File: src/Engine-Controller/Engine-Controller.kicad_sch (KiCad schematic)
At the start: 19 parts, among them J2 Jumper_NO, P3 3220-20-0200-00, U1 STM32H750VBTx, Y1 ECS-240-18-33-JGN-TR

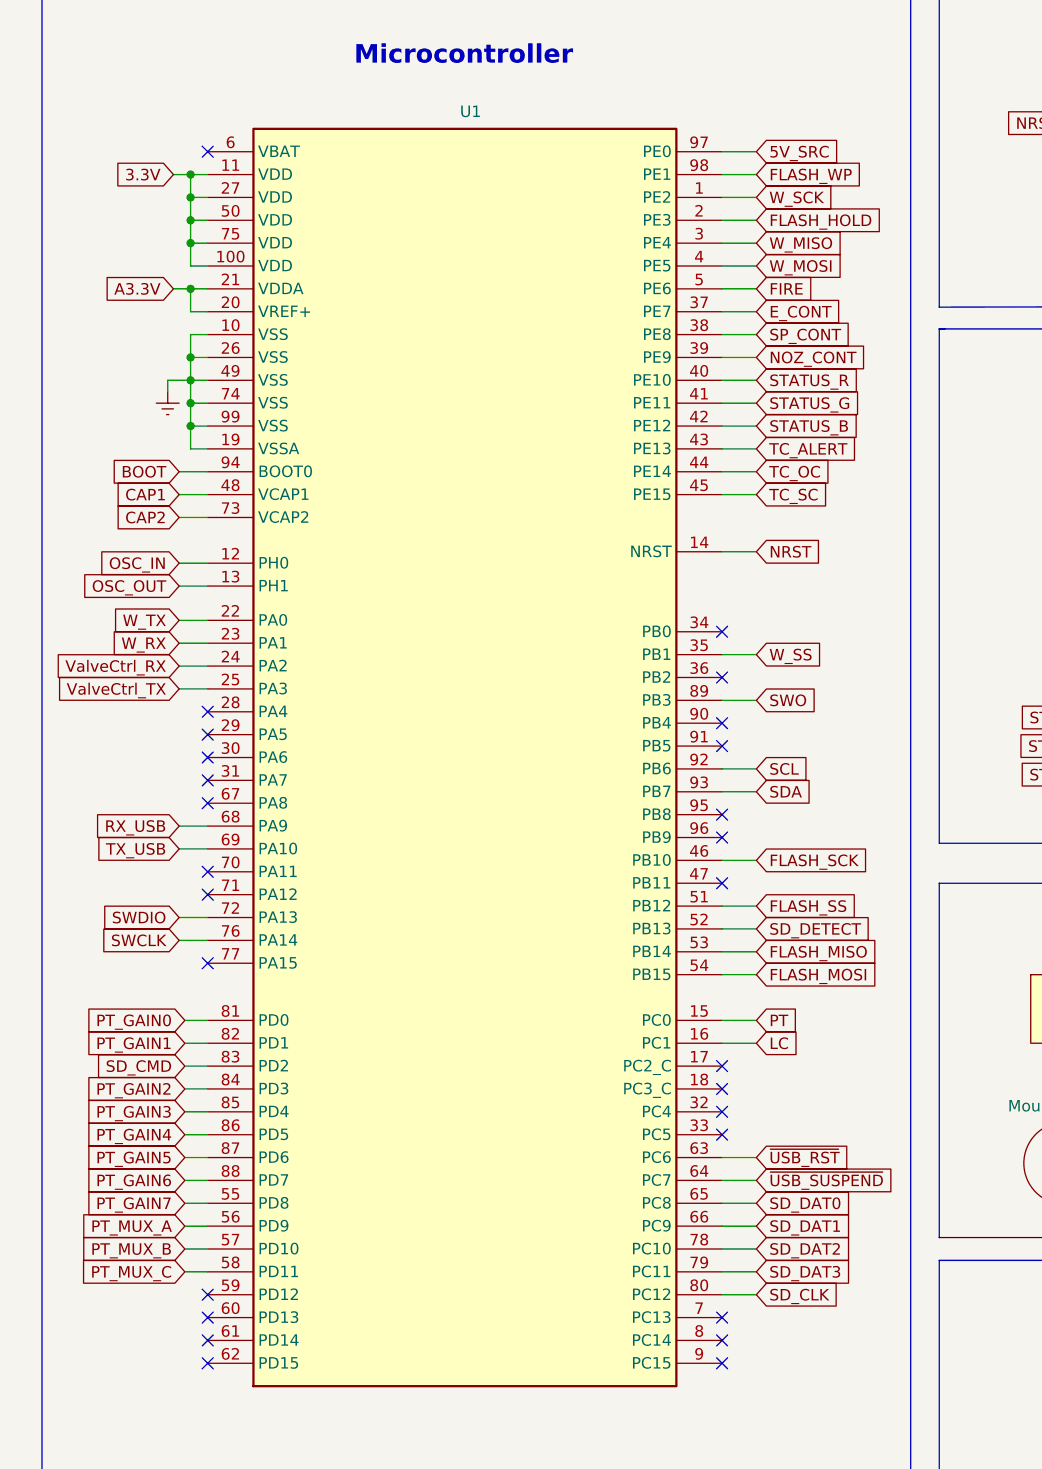
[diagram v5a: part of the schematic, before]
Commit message: removed uncessary caps from MCU LDO pins
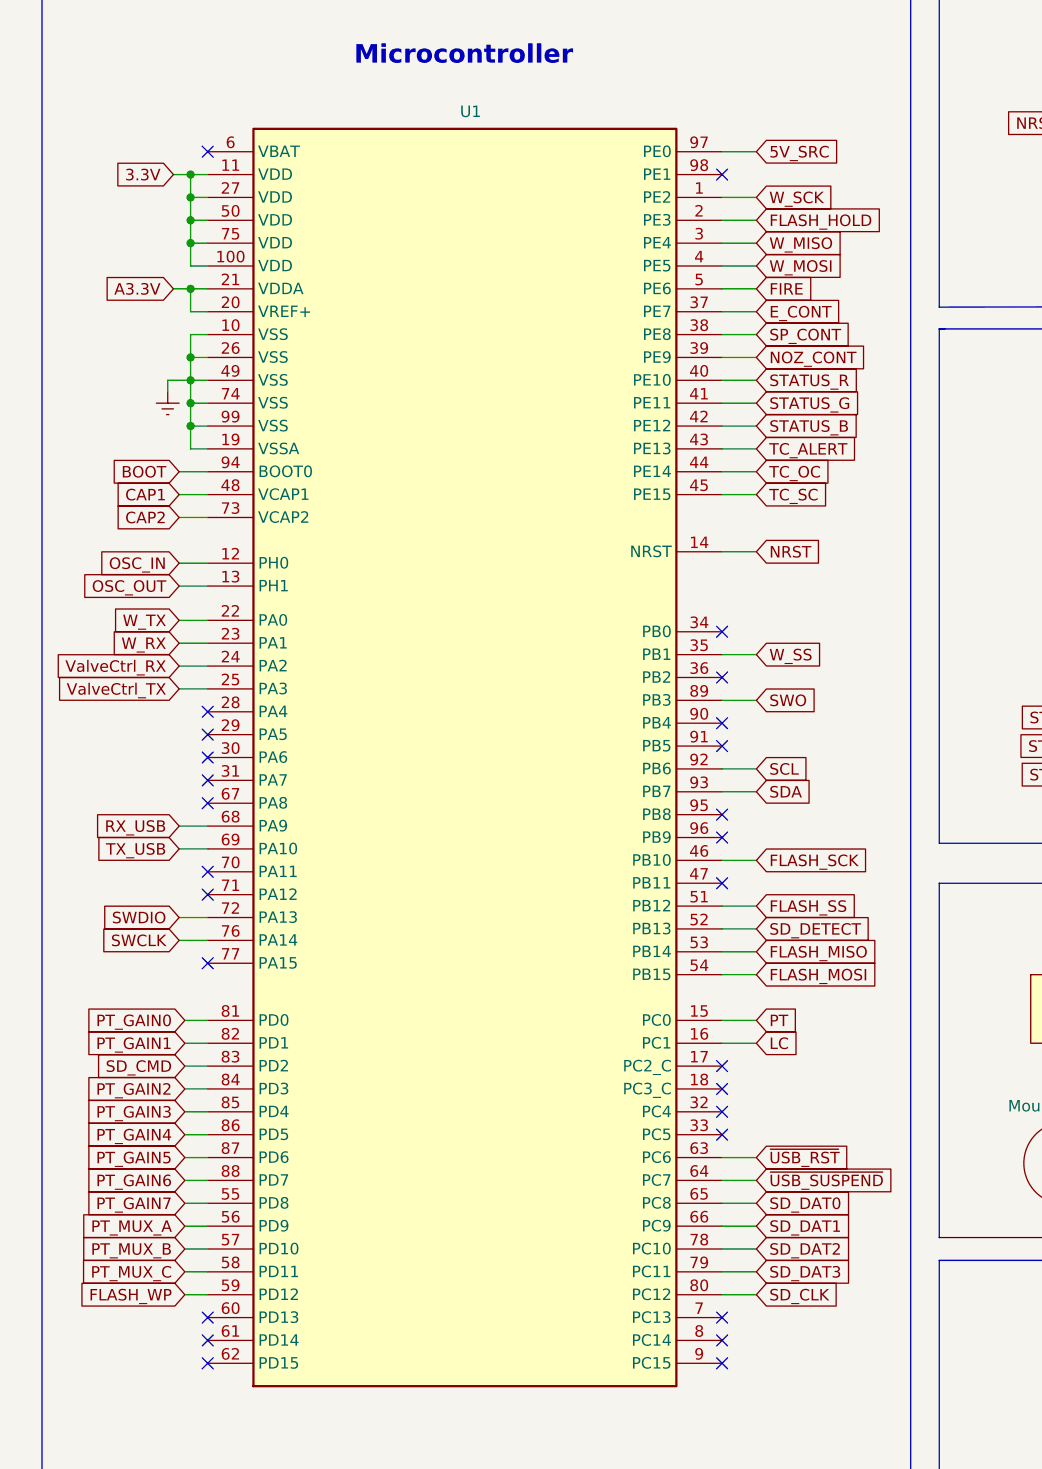
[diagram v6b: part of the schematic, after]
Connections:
- net FLASH_WP: now also U1.59 (PD12); no longer U1.98 (PE1)
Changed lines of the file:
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@@
   (no_connect (at 34.29 106.68))
   (no_connect (at 34.29 111.76))
+  (no_connect (at 91.44 41.91))
   (no_connect (at 91.44 113.03))
-  (no_connect (at 34.29 166.37))
   (no_connect (at 160.655 43.815))
   (no_connect (at 160.655 36.195))
@@
     (stroke (width 0) (type default) (color 0 0 0 0))
   )
-  (wire (pts (xy 91.44 41.91) (xy 95.25 41.91))
-    (stroke (width 0) (type default) (color 0 0 0 0))
-  )
   (wire (pts (xy 201.295 97.155) (xy 204.47 97.155))
     (stroke (width 0) (type default) (color 0 0 0 0))
@@
   )
   (wire (pts (xy 91.44 67.31) (xy 95.25 67.31))
+    (stroke (width 0) (type default) (color 0 0 0 0))
+  )
+  (wire (pts (xy 31.75 166.37) (xy 34.29 166.37))
     (stroke (width 0) (type default) (color 0 0 0 0))
   )
@@
     )
   )
-  (global_label "FLASH_WP" (shape input) (at 95.25 41.91 0) (fields_autoplaced)
-    (effects (font (size 1.27 1.27)) (justify left))
-    (property "Intersheet References" "${INTERSHEET_REFS}" (id 0) (at -43.18 5.08 0)
+  (global_label "FLASH_WP" (shape input) (at 31.75 166.37 180) (fields_autoplaced)
+    (effects (font (size 1.27 1.27)) (justify right))
+    (property "Intersheet References" "${INTERSHEET_REFS}" (id 0) (at 170.18 203.2 0)
       (effects (font (size 1.27 1.27)) hide)
     )
@@
       (reference "#PWR0109") (unit 1) (value "Earth") (footprint "")
     )
+    (path "/00000000-0000-0000-0000-000060d7f309/59b043bf-a20d-42bd-97fc-7a18b415d9ac"
+      (reference "#PWR?") (unit 1) (value "Earth") (footprint "")
+    )
+    (path "/00000000-0000-0000-0000-000060d7f309/64a6fbd3-18d0-41d3-87fa-96e96c558542"
+      (reference "#PWR?") (unit 1) (value "Earth") (footprint "")
+    )
     (path "/00000000-0000-0000-0000-0000610156a4"
       (reference "B1") (unit 1) (value "PTS647SM38SMTR2LFS") (footprint "Engine-Controller:PTS647SM38SMTR2LFS")
@@
       (reference "C23") (unit 1) (value "2.2uF") (footprint "Engine-Controller:CAP_0603")
     )
-    (path "/00000000-0000-0000-0000-000060d7f309/b8efbc02-3ff5-4b40-a4ff-aeeb345b51c7"
-      (reference "C24") (unit 1) (value "2.2uF") (footprint "Engine-Controller:CAP_0603")
-    )
-    (path "/00000000-0000-0000-0000-000060d7f309/3782e2ce-c2e6-4a26-97ce-a9ab47298b0b"
-      (reference "C25") (unit 1) (value "2.2uF") (footprint "Engine-Controller:CAP_0603")
-    )
     (path "/00000000-0000-0000-0000-000060d7f309/24701c54-6890-4a0a-8a9b-3ce9dde41556"

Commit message: removed uneccessary info from footprint lib files
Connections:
- net Earth: now also B1.1; no longer B1.3
- net NRST: now also B1.3; no longer B1.1
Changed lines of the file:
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@@
       (reference "#PWR0101") (unit 1) (value "Earth") (footprint "")
+    )
+    (path "/00000000-0000-0000-0000-000060d7f309/64a6fbd3-18d0-41d3-87fa-96e96c558542"
+      (reference "#PWR0102") (unit 1) (value "Earth") (footprint "")
     )
     (path "/00000000-0000-0000-0000-000060d7f309/00000000-0000-0000-0000-000060ec7bcd"
@@
     )
     (path "/00000000-0000-0000-0000-000060d7f309/59b043bf-a20d-42bd-97fc-7a18b415d9ac"
-      (reference "#PWR?") (unit 1) (value "Earth") (footprint "")
-    )
-    (path "/00000000-0000-0000-0000-000060d7f309/64a6fbd3-18d0-41d3-87fa-96e96c558542"
-      (reference "#PWR?") (unit 1) (value "Earth") (footprint "")
+      (reference "#PWR0110") (unit 1) (value "Earth") (footprint "")
+    )
+    (path "/00000000-0000-0000-0000-000060d7f309/119a8479-8714-4870-96ff-5e05b79ae5ba"
+      (reference "#PWR0111") (unit 1) (value "Earth") (footprint "")
     )
     (path "/00000000-0000-0000-0000-0000610156a4"
@@
     )
     (path "/00000000-0000-0000-0000-000060d7f309/00000000-0000-0000-0000-0000611c3d38"
-      (reference "C6") (unit 1) (value "10uF") (footprint "Engine-Controller:CWR11HH106KB")
+      (reference "C6") (unit 1) (value "10uF") (footprint "Engine-Controller:T491A106K010AT")
     )
     (path "/00000000-0000-0000-0000-000060d7f309/00000000-0000-0000-0000-0000611c7d2a"
-      (reference "C7") (unit 1) (value "10uF") (footprint "Engine-Controller:CWR11HH106KB")
+      (reference "C7") (unit 1) (value "10uF") (footprint "Engine-Controller:T491A106K010AT")
     )
     (path "/00000000-0000-0000-0000-000060de014c"
@@
     )
     (path "/00000000-0000-0000-0000-000060d7f309/1d006bfc-4557-4b0f-907a-1f43e64bc9f4"
-      (reference "C27") (unit 1) (value "10uF") (footprint "Engine-Controller:CWR11HH106KB")
+      (reference "C27") (unit 1) (value "10uF") (footprint "Engine-Controller:T491A106K010AT")
     )
     (path "/00000000-0000-0000-0000-000060d7f309/5718e2f7-461b-45e2-ad3c-f721d4232866"
-      (reference "C28") (unit 1) (value "10uF") (footprint "Engine-Controller:CWR11HH106KB")
+      (reference "C28") (unit 1) (value "10uF") (footprint "Engine-Controller:T491A106K010AT")
     )
     (path "/d060135e-4b32-4403-ae1a-9301174376e1/a10ee6ff-8c81-411f-9ad3-221b7916e886"
@@
     )
     (path "/00000000-0000-0000-0000-000060d7f309/00000000-0000-0000-0000-000061e22a22"
-      (reference "U3") (unit 1) (value "LMS8117AMP-3.3_NOPB") (footprint "Engine-Controller:SOT-223")
+      (reference "U3") (unit 1) (value "LMS8117AMP-3.3_NOPB") (footprint "Engine-Controller:LMS8117AMP-3.3NOPB")
     )
     (path "/9f3f32e1-1873-42fa-9cca-aa278e3c01ec/552318ff-73f8-43e9-bc5a-0ad33868b553"
@@
     )
     (path "/00000000-0000-0000-0000-000060d7f309/2c73e679-5bfa-442d-b4e4-4c862a7c2a9e"
-      (reference "U10") (unit 1) (value "LMS8117AMP-3.3_NOPB") (footprint "Engine-Controller:SOT-223")
+      (reference "U10") (unit 1) (value "LMS8117AMP-3.3_NOPB") (footprint "Engine-Controller:LMS8117AMP-3.3NOPB")
     )
     (path "/9f3f32e1-1873-42fa-9cca-aa278e3c01ec/53fc9498-09c7-40bc-a046-dea2644e2b0f"

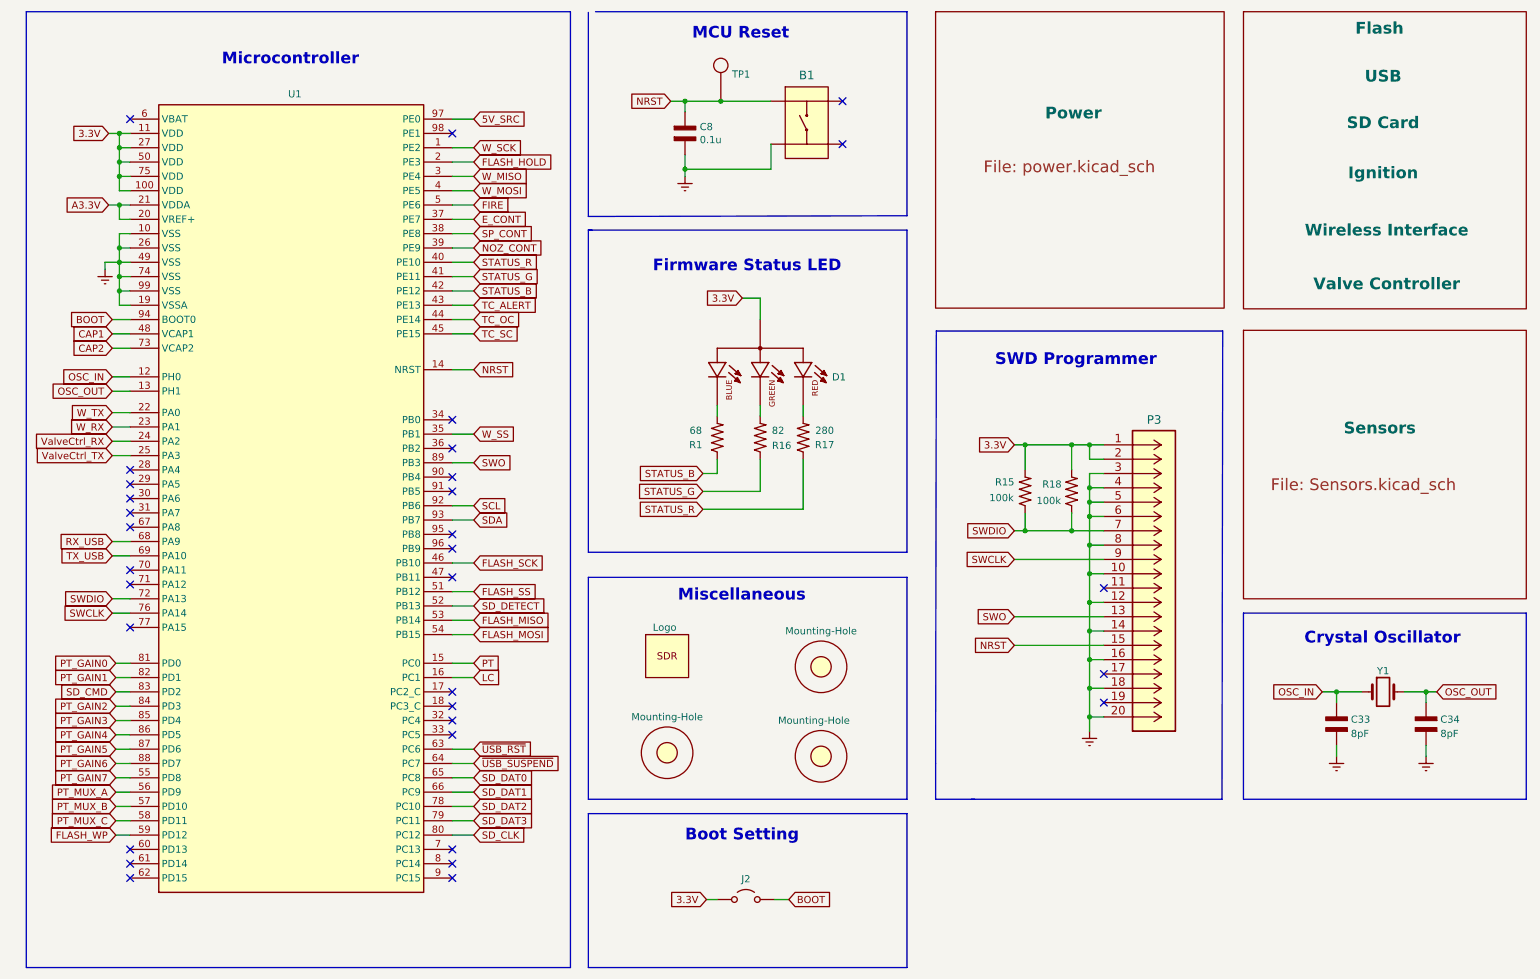
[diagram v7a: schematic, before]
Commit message: added load resistors to amplifier outputs
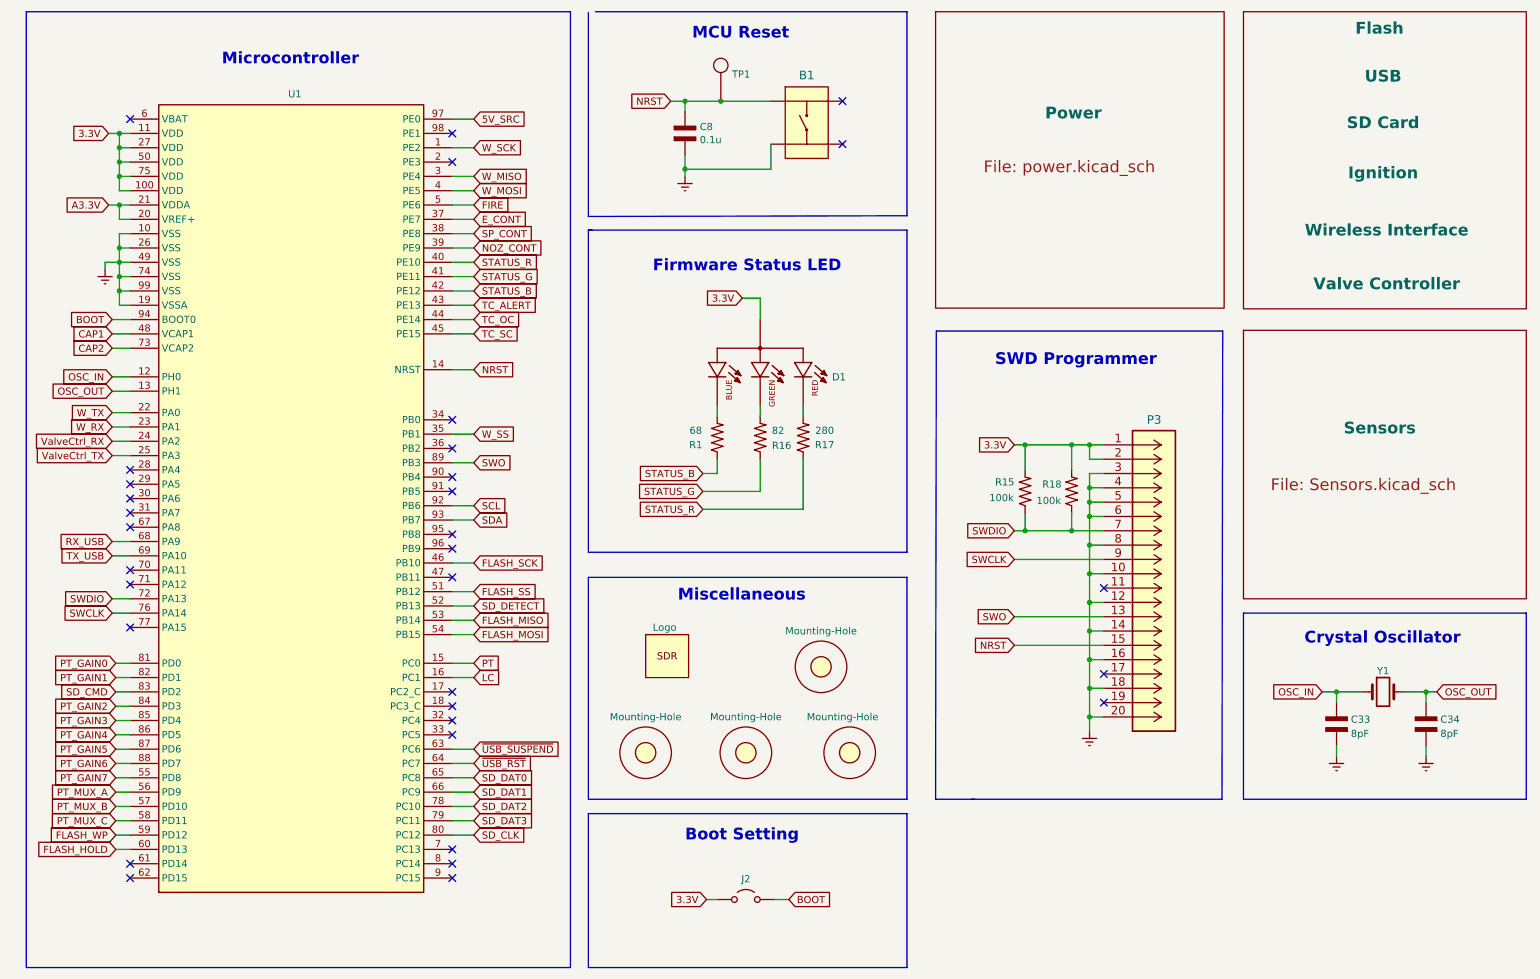
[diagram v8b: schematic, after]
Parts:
- added H1: Mounting-Hole, Engine-Controller:MountingHole_4.3mm_M4_DIN965, symbol Engine-Controller:Mounting-Hole
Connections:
- net FLASH_HOLD: now also U1.60 (PD13); no longer U1.2 (PE3)
- net ~{USB_RST}: now also U1.64 (PC7); no longer U1.63 (PC6)
- net ~{USB_SUSPEND}: now also U1.63 (PC6); no longer U1.64 (PC7)
